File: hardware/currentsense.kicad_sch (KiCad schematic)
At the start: 12 parts, among them U701 MAX49925, U703 MAX49925

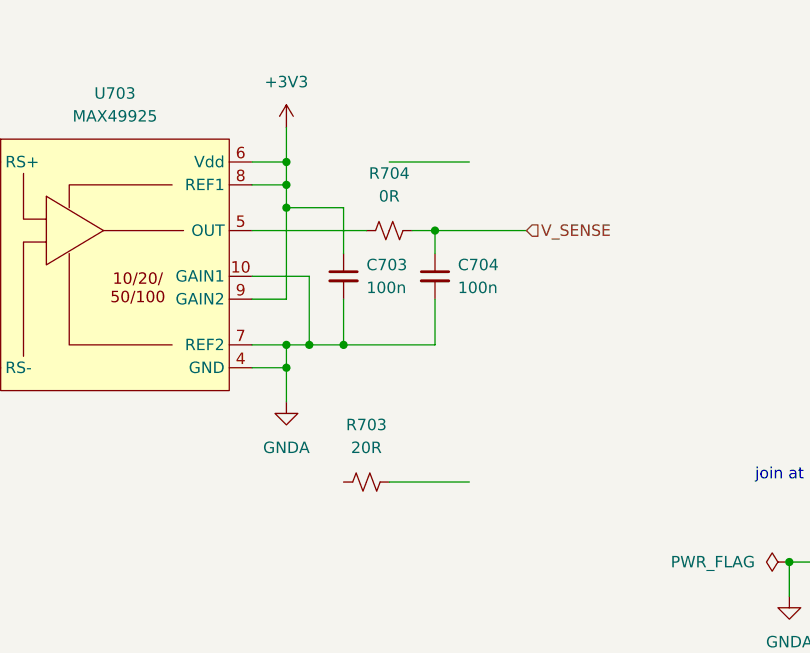
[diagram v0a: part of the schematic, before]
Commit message: change inductor footprint, add I2C1 SCL on user 3
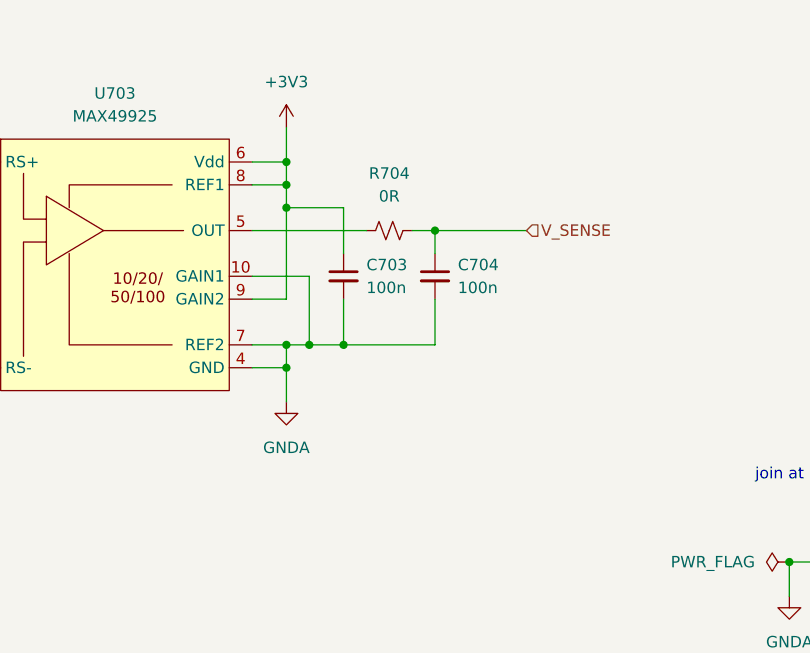
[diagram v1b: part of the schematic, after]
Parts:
- removed R703: 20R, Resistor_SMD:R_0402_1005Metric, symbol Device:R_Small_US
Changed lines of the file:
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@@
-    (stroke (width 0) (type default))
-  )
-  (wire (pts (xy 148.59 127) (xy 157.48 127))
     (stroke (width 0) (type default))
   )
@@
     (stroke (width 0) (type default))
   )
-  (wire (pts (xy 148.59 91.44) (xy 157.48 91.44))
-    (stroke (width 0) (type default))
-  )
   (text "join at power connector" (at 189.23 127 0)
     (effects (font (size 1.27 1.27)) (justify left bottom))
@@
     (effects (font (size 1.27 1.27)) (justify right))
   )
-  (symbol (lib_id "Device:R_Small_US") (at 146.05 127 90) (unit 1)
-    (in_bom yes) (on_board yes) (dnp no) (fields_autoplaced)
-    (property "Reference" "R703" (at 146.05 120.65 90)
-      (effects (font (size 1.27 1.27)))
-    )
-    (property "Value" "20R" (at 146.05 123.19 90)
-      (effects (font (size 1.27 1.27)))
-    )
-    (property "Footprint" "Resistor_SMD:R_0402_1005Metric" (at 146.05 127 0)
-      (effects (font (size 1.27 1.27)) hide)
-    )
-    (property "Datasheet" "~" (at 146.05 127 0)
-      (effects (font (size 1.27 1.27)) hide)
-    )
-    (pin "1")
-    (pin "2")
-    (instances
-      (project "lemon-pepper"
-        (path "/0306e2fa-4433-4288-91d9-65a3484207ad/41d11f3b-333a-47c0-a126-1f991ee11e83"
-          (reference "R703") (unit 1)
-        )
-      )
-    )
-  )
   (symbol (lib_id "power:PWR_FLAG") (at 193.04 135.89 90) (unit 1)

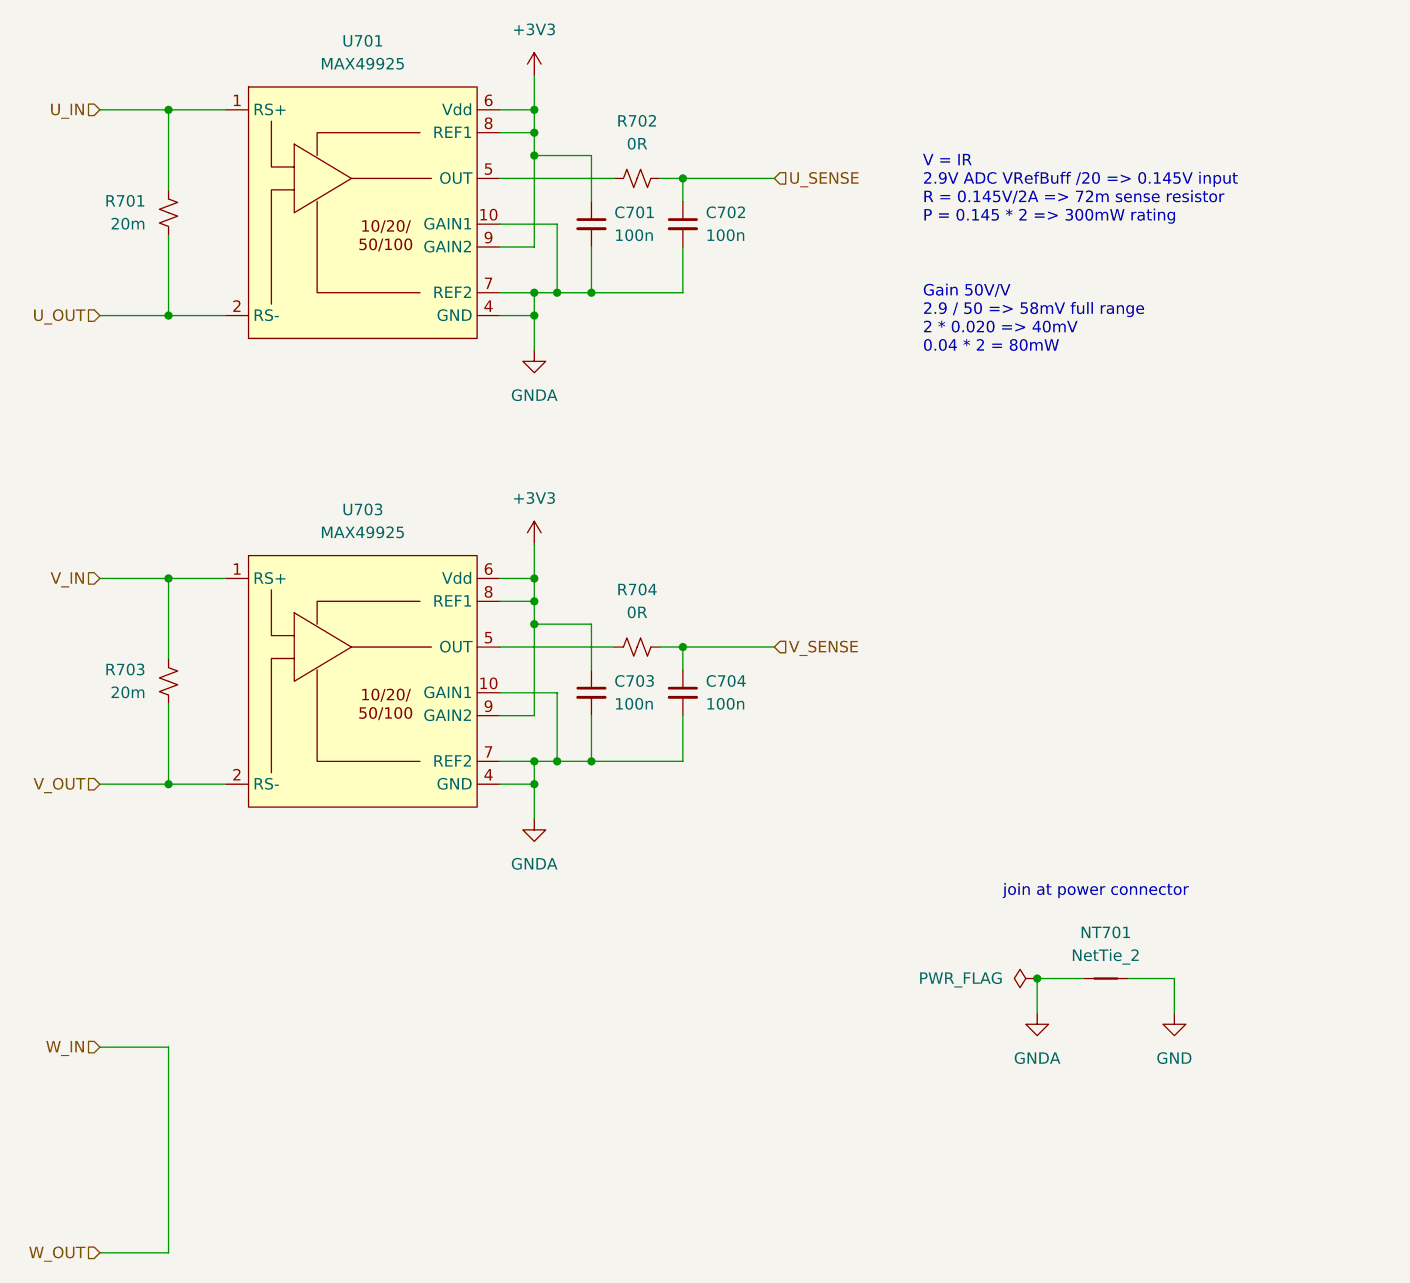
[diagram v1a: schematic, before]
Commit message: Made analog gain of current sense amps selectable by mcu. Removed analog ground plane and tied all grounds together
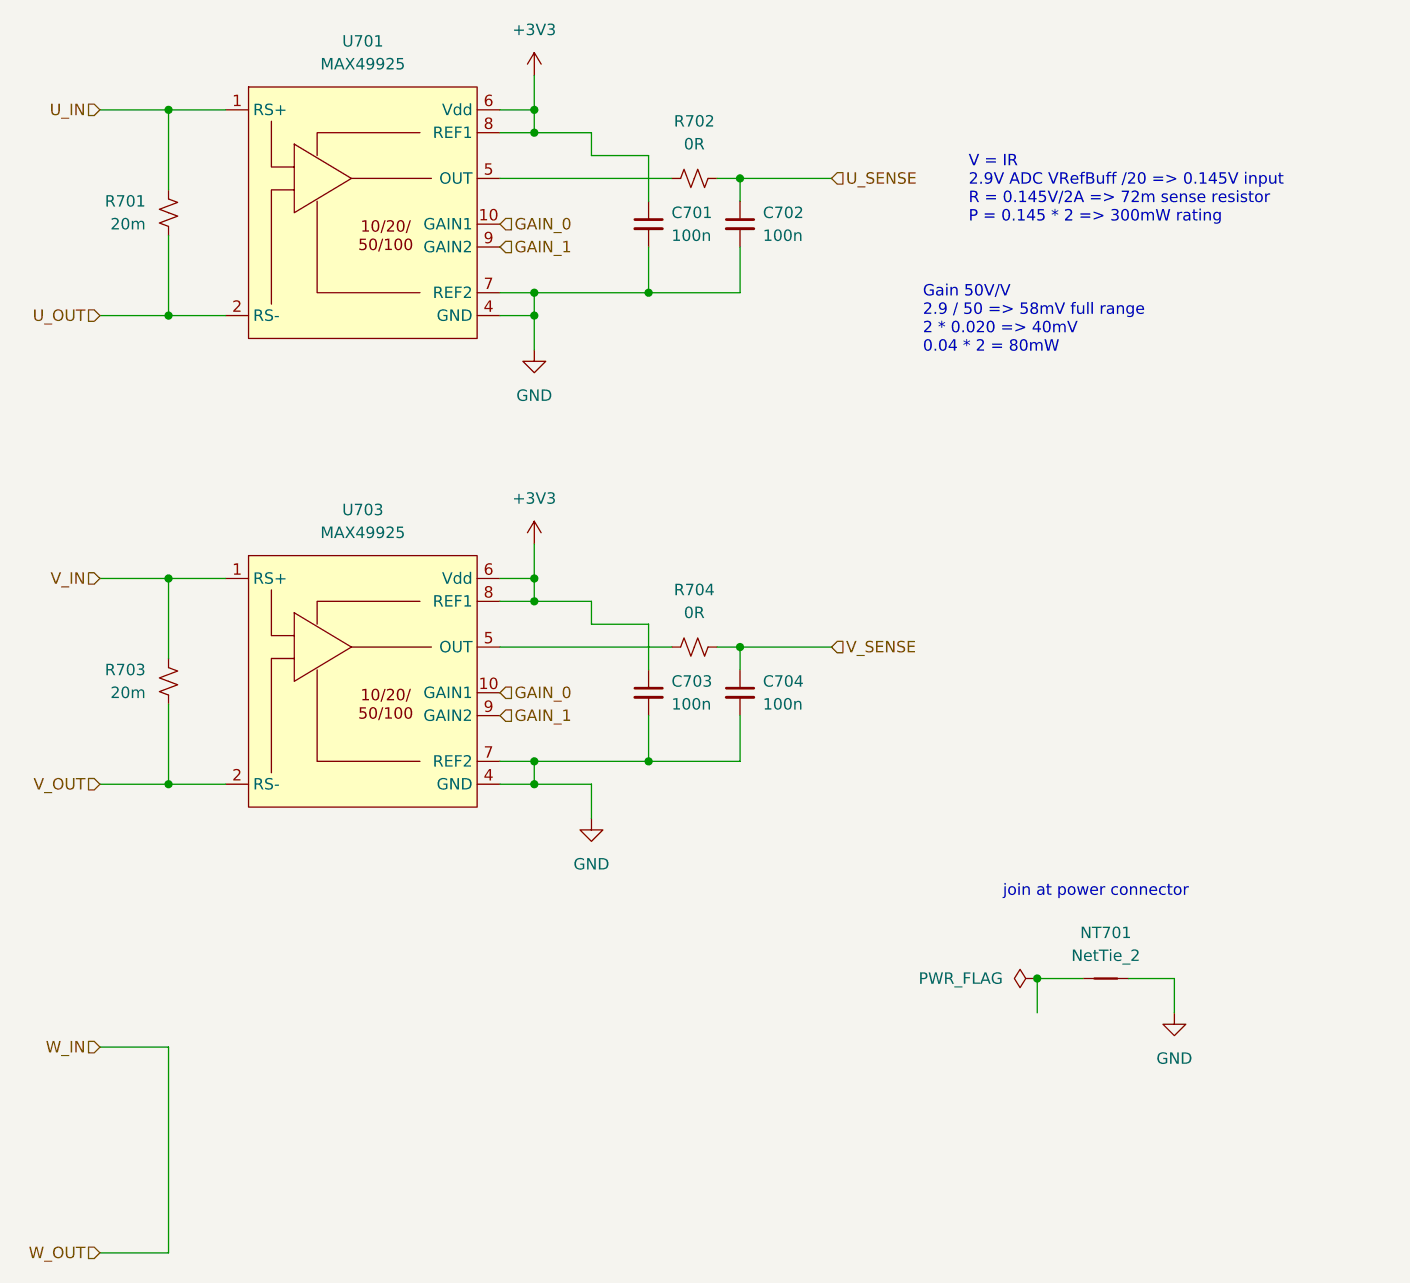
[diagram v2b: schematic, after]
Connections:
- net +3V3: no longer U701.9 (GAIN2), U703.9 (GAIN2)
- net GND: now also C701.2, C702.2, C703.2, C704.2, U701.11 (EP), U701.4 (GND), U701.7 (REF2), U703.11 (EP), U703.4 (GND), U703.7 (REF2)
- removed net GNDA: C701.2, C702.2, C703.2, C704.2, NT701.1, U701.10 (GAIN1), U701.11 (EP), U701.4 (GND), U701.7 (REF2), U703.10 (GAIN1), U703.11 (EP), U703.4 (GND), U703.7 (REF2)
- new net GAIN_0: U701.10 (GAIN1), U703.10 (GAIN1)
- new net GAIN_1: U701.9 (GAIN2), U703.9 (GAIN2)
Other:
- moved on the sheet: C701, C702, C703, C704, R702, R704

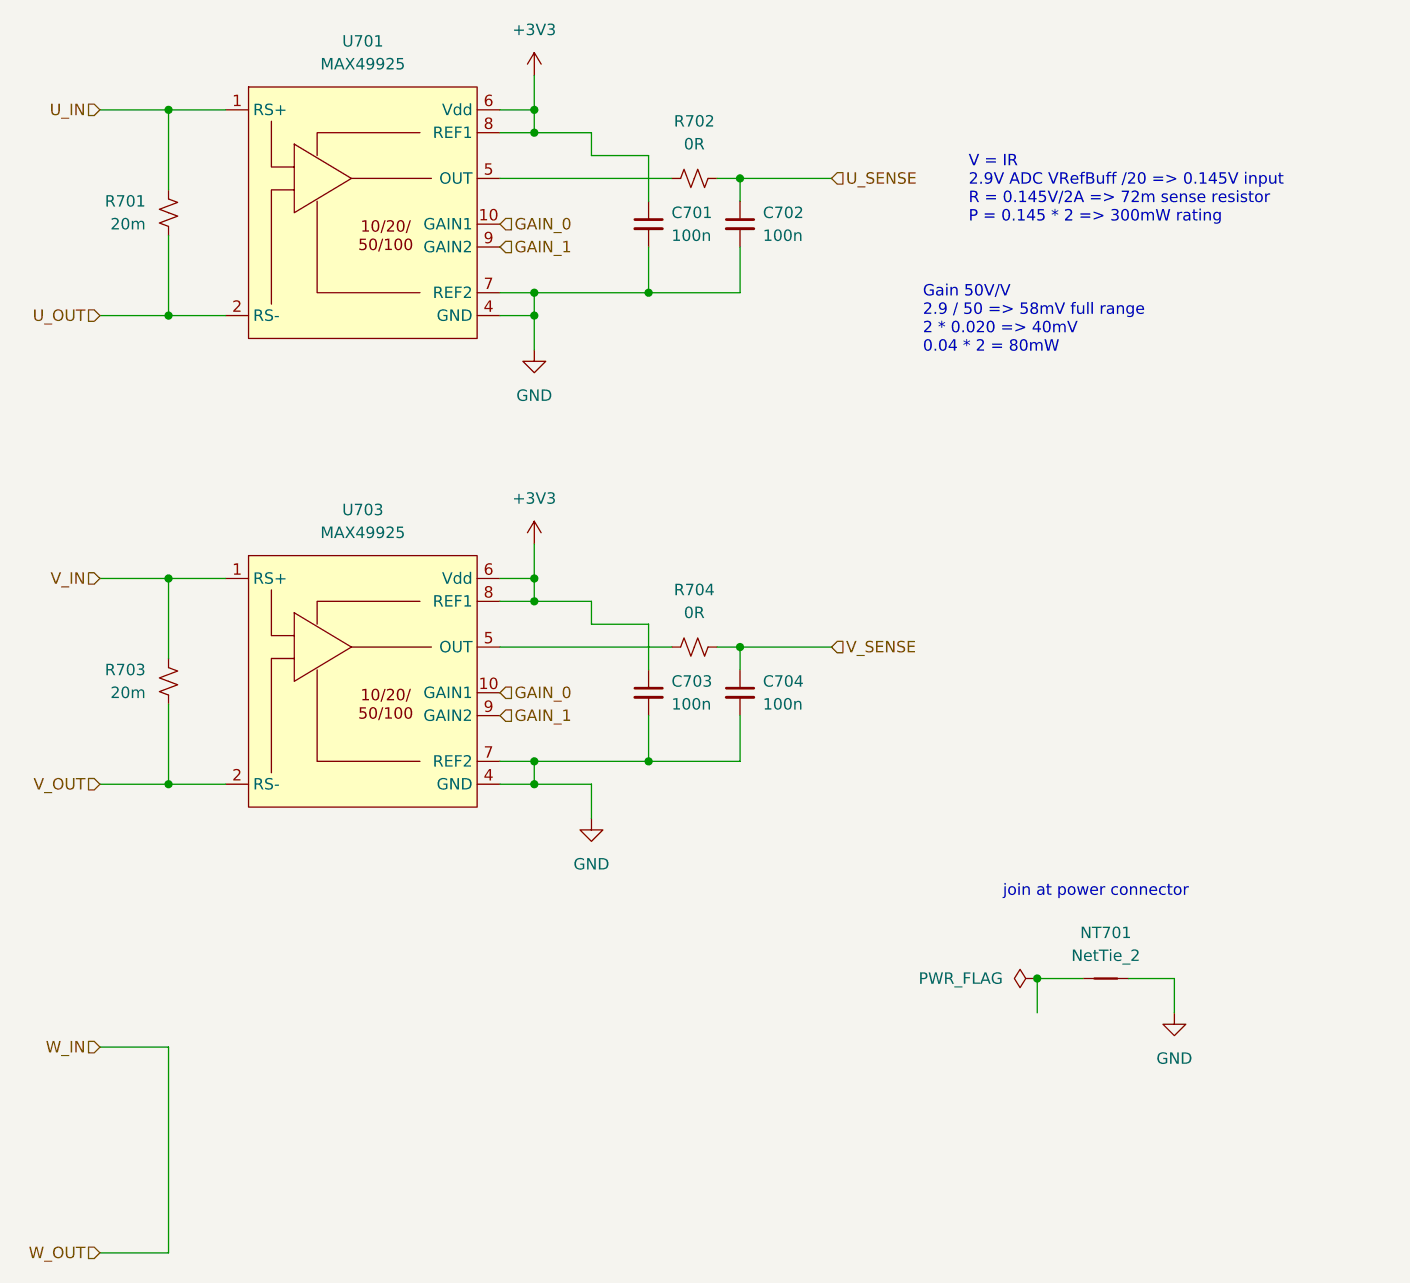
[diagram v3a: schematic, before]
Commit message: fix current sense pinout
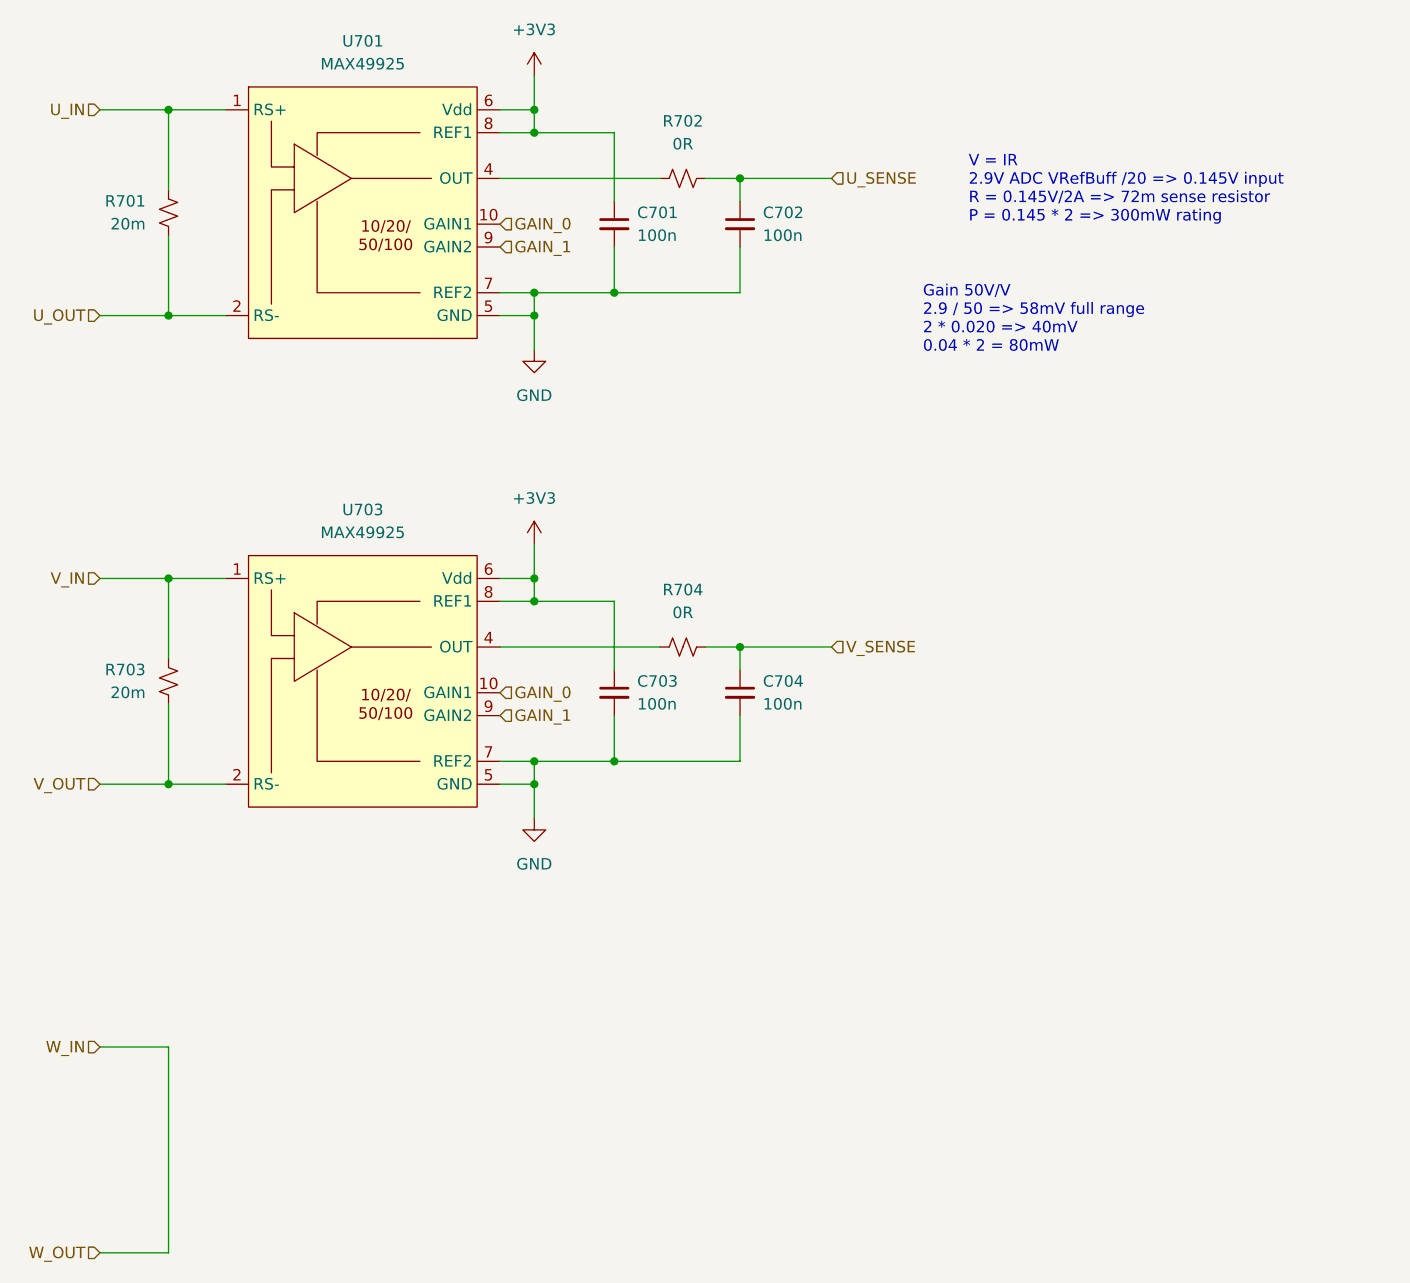
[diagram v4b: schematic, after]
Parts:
- removed NT701: NetTie_2, NetTie:NetTie-2_SMD_Pad0.5mm, symbol Device:NetTie_2
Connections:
- net GND: now also U701.5 (GND), U703.5 (GND); no longer U701.4 (GND), U703.4 (GND)
- net at R702.1: now also U701.4 (OUT); no longer U701.5 (OUT)
- net at R704.1: now also U703.4 (OUT); no longer U703.5 (OUT)
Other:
- note removed: "join at power connector"
- moved on the sheet: C701, C703, R702, R704

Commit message: Update BOM field LCSC ID
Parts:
- C701, C702, C703, C704: LCSC ID (none) -> C307331; LCSC Part C307331 -> (none)
- R701, R703: LCSC ID (none) -> C393094; LCSC Part C393094 -> (none)
- R702, R704: LCSC ID (none) -> C17168; LCSC Part C17168 -> (none)
- U701, U703: LCSC ID (none) -> C19193612; LCSC Part C19193612 -> (none)
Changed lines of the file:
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@@
 			)
 		)
-		(property "LCSC Part" "C307331"
+		(property "LCSC ID" "C307331"
 			(at 160.02 52.07 0)
 			(effects
@@
 			)
 		)
-		(property "LCSC Part" "C17168"
+		(property "LCSC ID" "C17168"
 			(at 153.67 46.99 0)
 			(effects
@@
 			)
 		)
-		(property "LCSC Part" "C19193612"
+		(property "LCSC ID" "C19193612"
 			(at 118.11 49.53 0)
 			(effects
@@
 			)
 		)
-		(property "LCSC Part" "C393094"
+		(property "LCSC ID" "C393094"
 			(at 96.52 102.87 0)
 			(effects
@@
 			)
 		)
-		(property "LCSC Part" "C17168"
+		(property "LCSC ID" "C17168"
 			(at 153.67 99.06 0)
 			(effects
@@
 			)
 		)
-		(property "LCSC Part" "C307331"
+		(property "LCSC ID" "C307331"
 			(at 160.02 104.14 0)
 			(effects
@@
 			)
 		)
-		(property "LCSC Part" "C307331"
+		(property "LCSC ID" "C307331"
 			(at 146.05 104.14 0)
 			(effects
@@
 			)
 		)
-		(property "LCSC Part" "C19193612"
+		(property "LCSC ID" "C19193612"
 			(at 118.11 101.6 0)
 			(effects
@@
 			)
 		)
-		(property "LCSC Part" "C393094"
+		(property "LCSC ID" "C393094"
 			(at 96.52 50.8 0)
 			(effects
@@
 			)
 		)
-		(property "LCSC Part" "C307331"
+		(property "LCSC ID" "C307331"
 			(at 146.05 52.07 0)
 			(effects
